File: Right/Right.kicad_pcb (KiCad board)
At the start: 2 copper layers, 106 parts, among them SW1 SW_PUSH, SW10 SW_PUSH, SW100 SW_Push_Dual_R, SW101 SW_Push_Dual_R, SW102 SW_Push_Dual_R, SW11 SW_PUSH, SW12 SW_PUSH, SW13 SW_PUSH, SW14 SW_PUSH, SW15 SW_PUSH, SW16 SW_PUSH, SW17 SW_PUSH, SW18 SW_PUSH, SW19 SW_PUSH, SW2 SW_PUSH, SW20 SW_PUSH, SW200 SW_SPDT, SW21 SW_PUSH, SW22 SW_PUSH, SW23 SW_PUSH, SW24 SW_PUSH, SW25 SW_PUSH, SW26 SW_PUSH, SW27 SW_PUSH, SW28 SW_PUSH, SW29 SW_PUSH, SW3 SW_PUSH, SW30 SW_PUSH, SW31 SW_PUSH, SW32 SW_PUSH, SW33 SW_PUSH, SW34 SW_PUSH, SW35 SW_PUSH, SW36 SW_PUSH, SW37 SW_PUSH, SW38 SW_PUSH, SW39 SW_PUSH, SW4 SW_PUSH, SW40 SW_PUSH, SW41 SW_PUSH, SW42 SW_PUSH, SW43 SW_PUSH, SW44 SW_PUSH, SW45 SW_PUSH, SW5 SW_PUSH, SW6 SW_PUSH, SW7 SW_PUSH, SW8 SW_PUSH, SW9 SW_PUSH, U1 CH25-2032LF, U2 CH25-2032LF

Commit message: 小さく
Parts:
- moved D200 95.1 mm to (76.2, 78.1)
- moved D201 94.6 mm to (76.2, 73.0)
- moved U1 73.4 mm to (114.3, 53.3)
- moved U2 72.2 mm to (90.2, 53.3)
- moved SW102 66.7 mm to (206.5, 45.1)
- moved SW101 64.8 mm to (194.9, 45.1)
- moved SW100 62.9 mm to (183.5, 45.1)
- moved D102 47.9 mm to (197.5, 47.0), turned to 90 degrees
- moved C1 42.3 mm to (226.7, 69.2), turned to 270 degrees
- moved D101 39.1 mm to (186.1, 47.0), turned to 90 degrees
- moved D100 30.3 mm to (174.6, 47.0), turned to 90 degrees
- moved R1 24.8 mm to (216.5, 47.0)
- moved BPM1 20.4 mm to (209.6, 57.1)
- moved SW200 19.1 mm to (222.9, 43.2), turned to 180 degrees
- moved LED1 19.1 mm to (214.0, 43.2)
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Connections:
- BPM1 pad 14: col0 -> col7
- BPM1 pad 15: col1 -> col6
- BPM1 pad 16: col2 -> col5
- BPM1 pad 17: col3 -> col4
- BPM1 pad 18: col4 -> col3
- BPM1 pad 19: col5 -> col2
- BPM1 pad 20: col6 -> col1
- BPM1 pad 21: col7 -> col0
- SW100 pad 1: col0 -> col5
- SW101 pad 1: col1 -> col6
- SW102 pad 1: col2 -> col7
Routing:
- net col0: track 245.3 -> 394.1 mm
- net col4: track 148.4 -> 291.4 mm
- net col1: track 227.2 -> 359.0 mm
- net col2: track 207.7 -> 323.9 mm
- net col3: track 187.0 -> 302.2 mm
- net Net-(D200-Pad1): track 70.3 -> 183.0 mm
- net col6: track 145.2 -> 184.5 mm
- net col7: track 138.9 -> 175.4 mm
- net bat: track 64.0 -> 28.1 mm
- net rowsys: track 56.1 -> 25.7 mm
- net Net-(D200-Pad2): track 9.02 -> 36.9 mm
- net Net-(D100-Pad2): track 28.9 -> 9.42 mm
- net row5: track 299.7 -> 282.5 mm
- net row2: track 259.4 -> 242.3 mm
- net row4: track 281.5 -> 264.6 mm
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
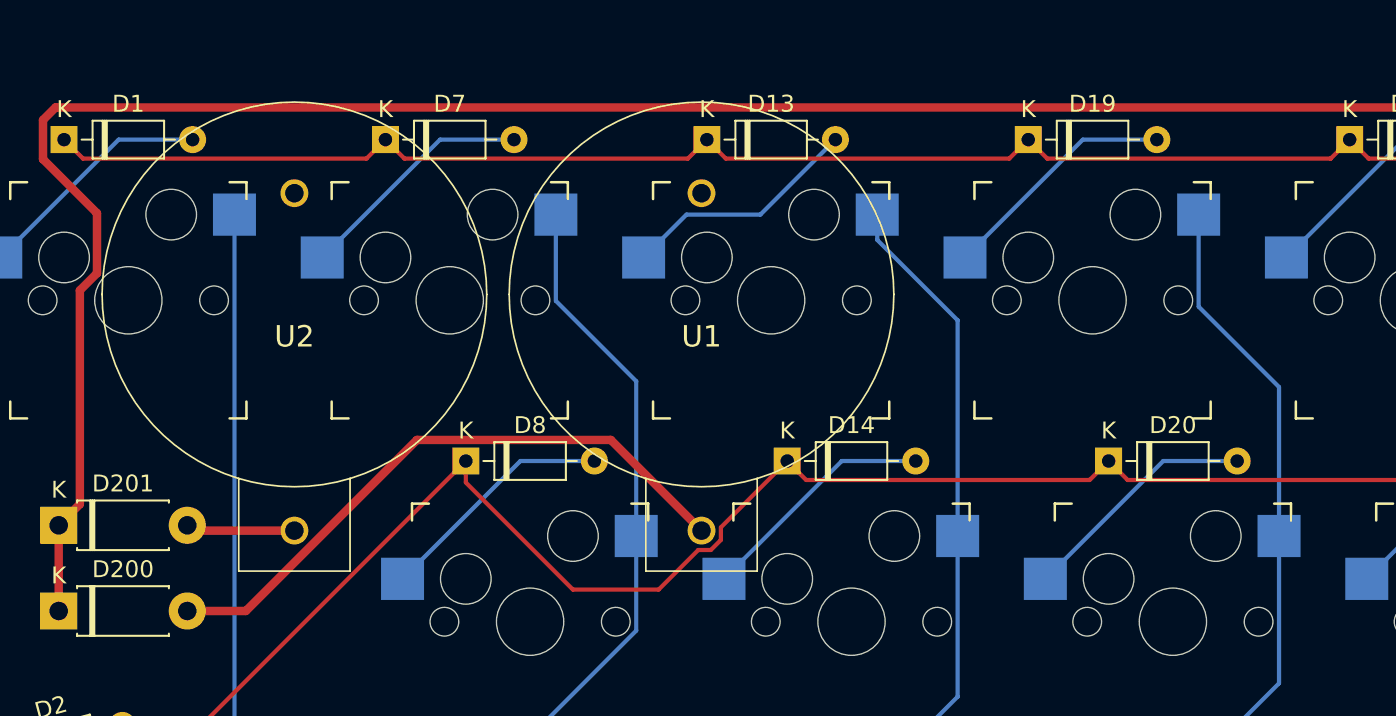
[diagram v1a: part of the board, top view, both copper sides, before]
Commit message: 電池位置調整
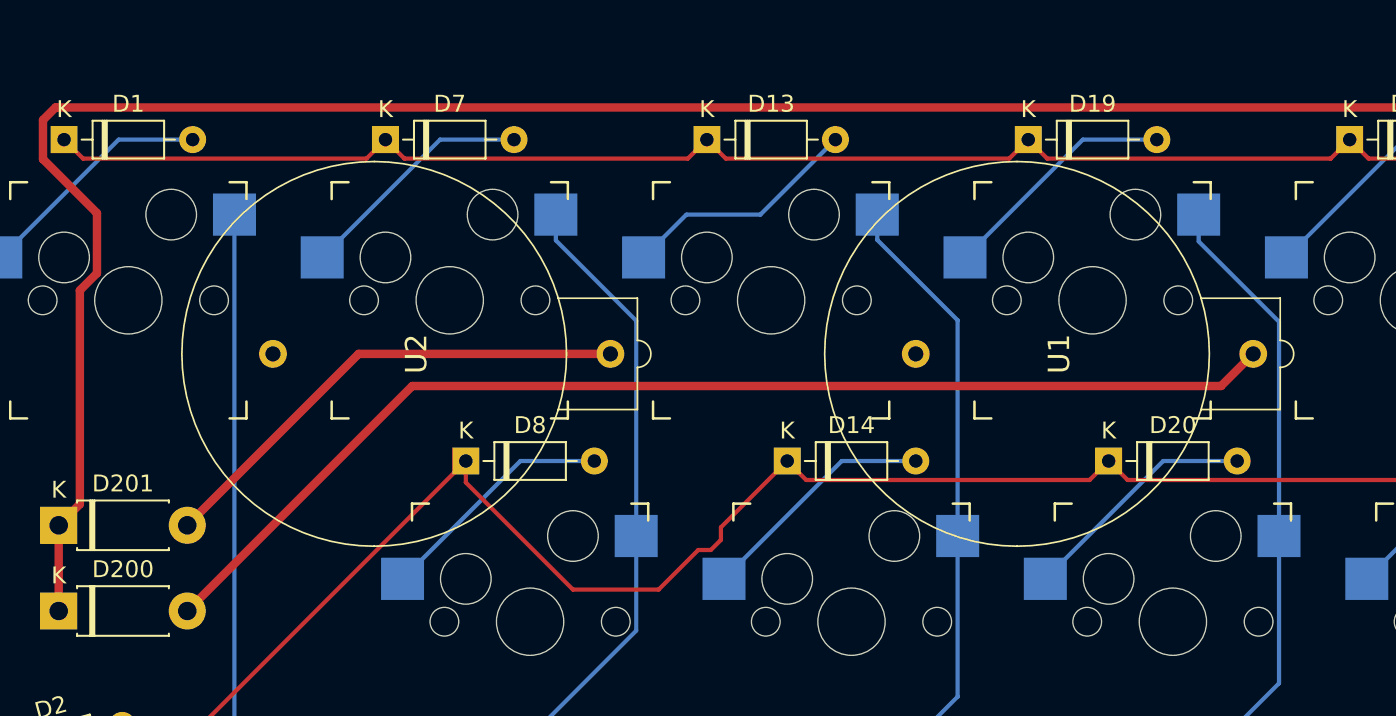
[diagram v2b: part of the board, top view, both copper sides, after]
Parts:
- moved U1 15.9 mm to (127.0, 62.9), turned to 90 degrees
- moved U2 9.61 mm to (88.9, 62.9), turned to 90 degrees
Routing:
- net Net-(D200-Pad2): track 36.9 -> 69.5 mm
- net Net-(D201-Pad2): track 6.48 -> 29.7 mm

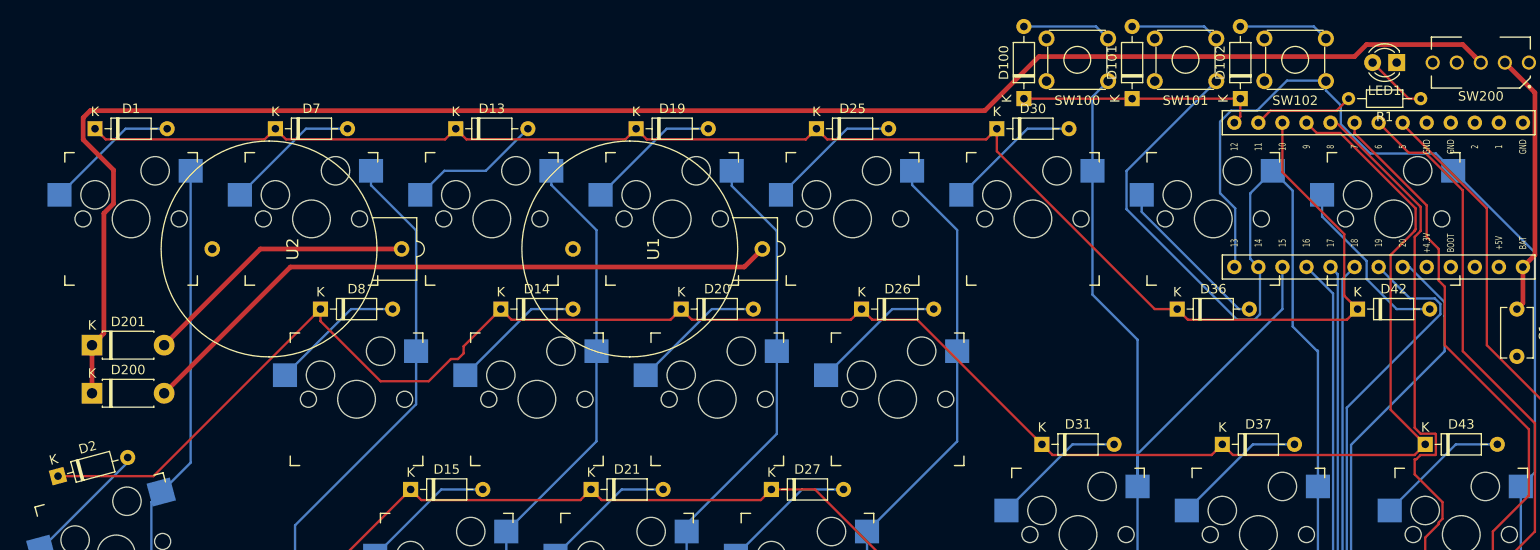
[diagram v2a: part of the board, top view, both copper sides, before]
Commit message: 配線整理
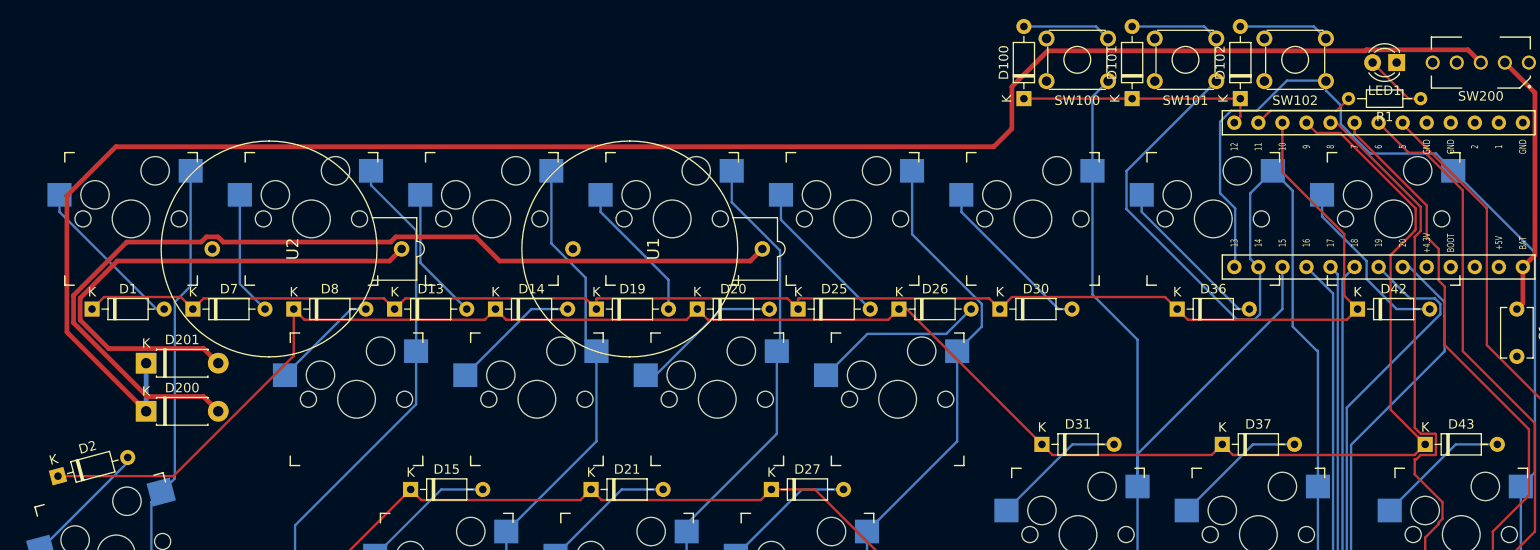
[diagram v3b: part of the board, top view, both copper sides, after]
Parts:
- moved D7 20.9 mm to (86.9, 69.2)
- moved D13 20.1 mm to (108.2, 69.2)
- moved D19 19.5 mm to (129.5, 69.2)
- moved D25 19.1 mm to (150.8, 69.2)
- moved D30 19.1 mm to (172.1, 69.2)
- moved D1 19.1 mm to (76.2, 69.2)
- moved D200 6.02 mm to (81.9, 80.0)
- moved D201 6.02 mm to (81.9, 74.9)
- moved D26 3.95 mm to (161.4, 69.2)
- moved D8 2.82 mm to (97.5, 69.2)
- moved D20 1.69 mm to (140.1, 69.2)
- moved D14 0.56 mm to (118.8, 69.2)
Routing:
- net Net-(D200-Pad2): track 69.5 -> 99.4 mm
- net Net-(D201-Pad2): track 29.7 -> 54.9 mm
- net Net-(D200-Pad1): track 183.0 -> 190.2 mm
- net row0: track 171.2 -> 164.6 mm
- net Net-(D26-Pad2): track 14.3 -> 18.2 mm
- net Net-(D30-Pad2): track 14.3 -> 17.7 mm
- net row1: track 211.7 -> 208.2 mm
- net Net-(D1-Pad2): track 14.3 -> 17.1 mm
- net Net-(D8-Pad2): track 14.3 -> 11.4 mm
- net col4: track 291.4 -> 293.6 mm
- net Net-(D25-Pad2): track 14.3 -> 16.0 mm
- net Net-(D20-Pad2): track 14.3 -> 16.0 mm
- net Net-(D7-Pad2): track 14.3 -> 13.2 mm
- net Net-(D19-Pad2): track 14.3 -> 15.0 mm
- net Net-(D14-Pad2): track 14.3 -> 13.7 mm

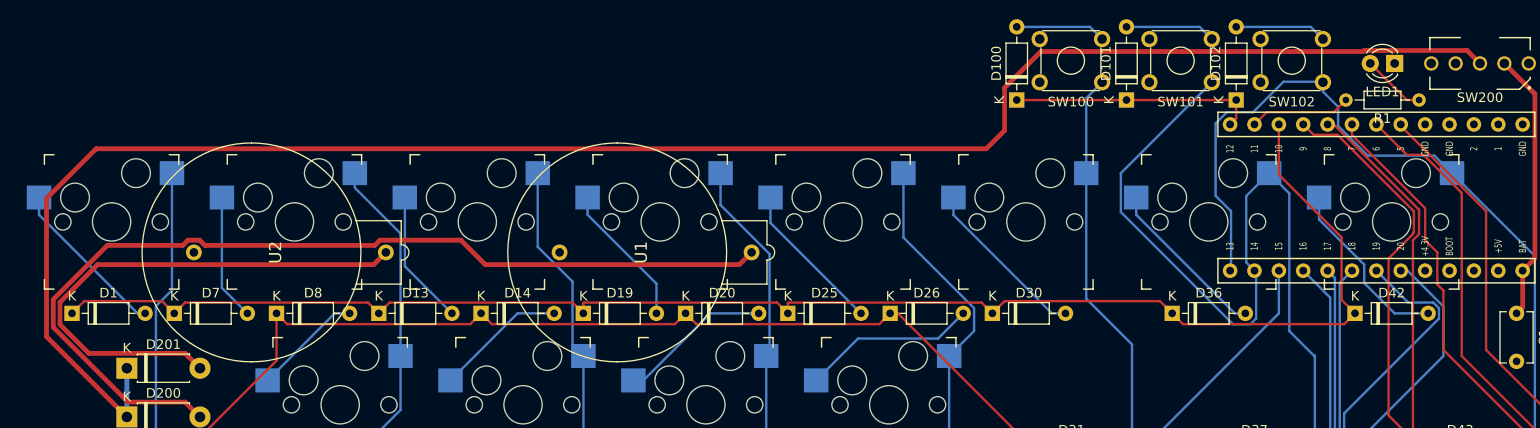
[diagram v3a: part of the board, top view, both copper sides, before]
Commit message: 配線に余裕をつくる
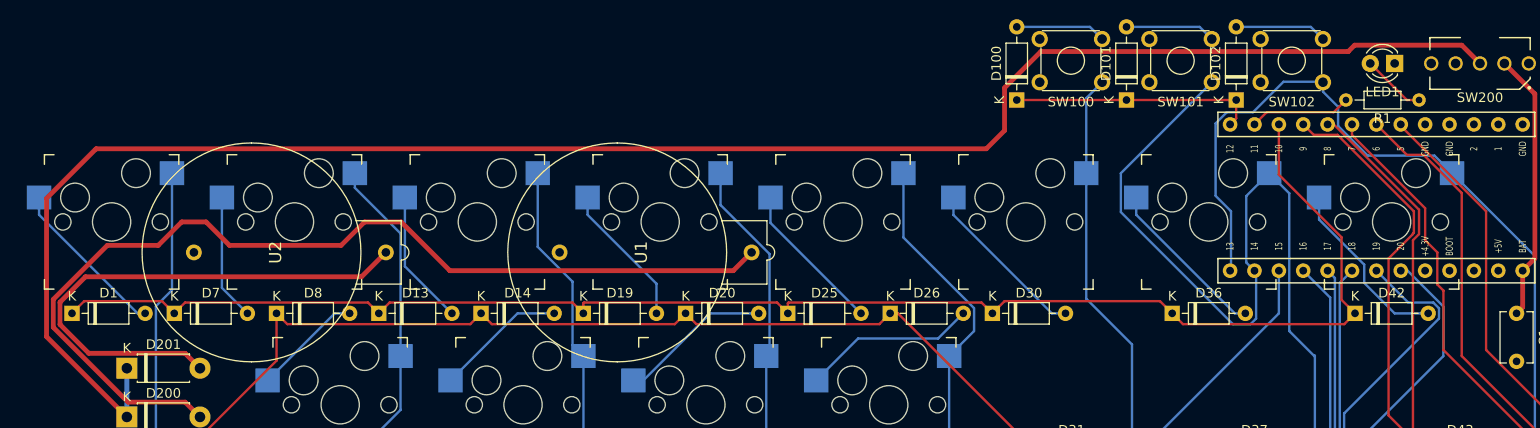
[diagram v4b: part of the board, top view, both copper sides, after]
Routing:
- net Net-(D200-Pad2): track 99.4 -> 103.1 mm

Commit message: 位置調整
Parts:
- BPM1: footprint mylibrary:BLEMicroPro_reversed -> mylibrary:BLEMicroPro
- moved BPM1 2.54 mm to (209.6, 59.7)
- moved D100 2.54 mm to (174.6, 49.5)
- moved D101 2.54 mm to (186.1, 49.5)
- moved D102 2.54 mm to (197.5, 49.5)
- moved LED1 2.54 mm to (214.0, 45.7)
- moved R1 2.54 mm to (216.5, 49.5)
- moved SW100 2.54 mm to (183.5, 47.7)
- moved SW101 2.54 mm to (194.9, 47.7)
- moved SW102 2.54 mm to (206.5, 47.7)
- moved SW200 2.54 mm to (222.9, 45.7)
- moved D36 2.54 mm to (190.8, 71.8)
- moved D42 2.54 mm to (209.9, 71.8)
- moved C1 1.27 mm to (226.7, 70.5)
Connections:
- BPM1 pad 10: row1 -> col4
- BPM1 pad 11: row0 -> col5
- BPM1 pad 12: led -> col6
- BPM1 pad 13: rowsys -> col7
- BPM1 pad 14: col7 -> rowsys
- BPM1 pad 15: col6 -> led
- BPM1 pad 16: col5 -> row0
- BPM1 pad 17: col4 -> row1
- BPM1 pad 18: col3 -> row2
- BPM1 pad 19: col2 -> row3
- BPM1 pad 20: col1 -> row4
- BPM1 pad 21: col0 -> row5
- BPM1 pad 6: row5 -> col0
- BPM1 pad 7: row4 -> col1
- BPM1 pad 8: row3 -> col2
- BPM1 pad 9: row2 -> col3
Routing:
- net col6: track 184.5 -> 172.2 mm
- net col1: track 359.0 -> 349.5 mm
- net row2: track 242.3 -> 235.3 mm
- net row3: track 252.9 -> 247.2 mm
- net row1: track 208.2 -> 203.6 mm
- net row5: track 282.5 -> 278.3 mm
- net col7: track 175.4 -> 172.1 mm
- net row4: track 264.6 -> 261.5 mm
- net col0: track 394.1 -> 391.1 mm
- net col2: track 323.9 -> 321.3 mm
- net Net-(D200-Pad1): track 190.7 -> 188.1 mm
- net col4: track 293.6 -> 291.0 mm
- net col3: track 302.4 -> 299.9 mm
- net Net-(D36-Pad2): track 17.4 -> 19.3 mm
- net bat: track 28.1 -> 26.3 mm
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
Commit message: 外枠とスペーサー
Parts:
- added REF**: Spacer, mylibrary:Spacer, F.Cu at (151.8, 79.0)
- added REF**: Spacer, mylibrary:Spacer, F.Cu at (73.3, 52.7)
- added REF**: Spacer, mylibrary:Spacer, F.Cu at (73.3, 73.1)
- added REF**: Spacer, mylibrary:Spacer, F.Cu at (76.5, 188.0)
- added REF**: Spacer, mylibrary:Spacer, F.Cu at (230.2, 185.8)
- added REF**: Spacer, mylibrary:Spacer, F.Cu at (230.2, 123.8)
- added REF**: Spacer, mylibrary:Spacer, F.Cu at (69.5, 124.5)
- added REF**: Spacer, mylibrary:Spacer, F.Cu at (161.9, 176.3)
- added REF**: Spacer, mylibrary:Spacer, F.Cu at (167.0, 52.7)
- added REF**: Spacer, mylibrary:Spacer, F.Cu at (154.3, 114.9)
- added REF**: Spacer, mylibrary:Spacer, F.Cu at (73.3, 79.1)
- added REF**: Spacer, mylibrary:Spacer, F.Cu at (230.2, 79.0)
- added REF**: Spacer, mylibrary:Spacer, F.Cu at (230.2, 73.0)
- moved D3 9.53 mm to (77.5, 105.3)
- moved D19 5.08 mm to (134.5, 69.2)
- moved D20 5.08 mm to (145.2, 69.2)
- moved D1 5.08 mm to (81.3, 69.2)
- moved D13 5.08 mm to (113.2, 69.2)
- moved D14 5.08 mm to (123.9, 69.2)
- moved D7 5.08 mm to (91.9, 69.2)
- moved D8 5.08 mm to (102.6, 69.2)
- moved D25 5.08 mm to (155.9, 69.2)
- moved D26 5.08 mm to (166.5, 69.2)
- moved D30 5.08 mm to (177.2, 69.2)
- moved D6 4.76 mm to (84.5, 168.8)
- moved D4 4.76 mm to (73.3, 126.1)
- moved D9 4.76 mm to (91.3, 101.6)
- moved D45 1.59 mm to (217.8, 169.2)
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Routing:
- net Net-(D201-Pad2): track 54.9 -> 44.7 mm
- net row2: track 235.3 -> 225.3 mm
- net Net-(D3-Pad2): track 13.5 -> 23.4 mm
- net col2: track 321.3 -> 331.1 mm
- net col3: track 299.9 -> 308.4 mm
- net Net-(D200-Pad2): track 103.1 -> 95.0 mm
- net Net-(D20-Pad2): track 16.0 -> 22.1 mm
- net row5: track 278.3 -> 272.2 mm
- net Net-(D1-Pad2): track 17.1 -> 23.0 mm
- net Net-(D35-Pad2): track 14.3 -> 8.59 mm
- net row3: track 247.2 -> 242.1 mm
- net row0: track 166.3 -> 161.2 mm
- net Net-(D25-Pad2): track 16.0 -> 21.1 mm
- net Net-(D14-Pad2): track 13.7 -> 18.8 mm
- net Net-(D8-Pad2): track 11.4 -> 16.5 mm
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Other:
- board outline added: 169.9 x 150.5 mm

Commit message: 角丸
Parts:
- removed the REF** at (151.8, 79.0)
- removed the REF** at (73.3, 52.7)
- removed the REF** at (167.0, 52.7)
- removed the REF** at (230.2, 73.0)
- added REF**: Spacer, mylibrary:Spacer, F.Cu at (147.3, 52.2)
- added REF**: Spacer, mylibrary:Spacer, F.Cu at (172.1, 73.5)
- added REF**: Spacer, mylibrary:Spacer, F.Cu at (230.7, 73.5)
- added REF**: Spacer, mylibrary:Spacer, F.Cu at (72.8, 52.2)
- added REF**: Spacer, mylibrary:Spacer, F.Cu at (230.7, 52.2)
- added REF**: Spacer, mylibrary:Spacer, F.Cu at (172.1, 78.5)
- moved D100 30.7 mm to (184.2, 78.7)
- moved D102 30.4 mm to (189.2, 78.7)
- moved D101 29.2 mm to (186.7, 78.7)
- moved D36 16.0 mm to (204.5, 80.0), turned to 90 degrees
- moved D30 9.61 mm to (178.4, 78.7), turned to 90 degrees
- moved SW100 8.26 mm to (191.8, 47.7)
- moved SW101 5.72 mm to (200.7, 47.7)
- moved R1 3.18 mm to (219.7, 49.5)
- moved SW200 3.18 mm to (226.1, 45.7), turned to 0 degrees
- moved LED1 3.17 mm to (217.2, 45.7)
- moved SW102 3.03 mm to (209.6, 47.6)
- moved C1 1.42 mm to (226.1, 71.8), turned to 180 degrees
- moved REF** 0.71 mm to (230.7, 78.5)
- moved REF** 0.71 mm to (72.8, 78.6)
- moved REF** 0.71 mm to (72.8, 73.6)
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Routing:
- net Net-(D102-Pad2): track 9.57 -> 47.1 mm
- net Net-(D101-Pad2): track 9.42 -> 37.9 mm
- net Net-(D100-Pad2): track 9.42 -> 33.4 mm
- net col5: track 168.9 -> 189.8 mm
- net rowsys: track 25.7 -> 34.9 mm
- net row0: track 161.2 -> 169.7 mm
- net Net-(D36-Pad2): track 21.7 -> 28.0 mm
- net Net-(D200-Pad1): track 188.1 -> 192.7 mm
- net Net-(D30-Pad2): track 22.8 -> 18.3 mm
- net col6: track 176.6 -> 180.3 mm
- net bat: track 26.3 -> 29.7 mm
- net led: track 10.6 -> 13.8 mm
- net Net-(D201-Pad2): track 44.7 -> 46.1 mm
- net row1: track 205.9 -> 205.1 mm
- net col7: track 171.1 -> 171.6 mm
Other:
- board size 169.9 x 150.5 mm -> 169.8 x 149.7 mm
